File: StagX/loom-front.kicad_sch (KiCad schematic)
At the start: 11 parts

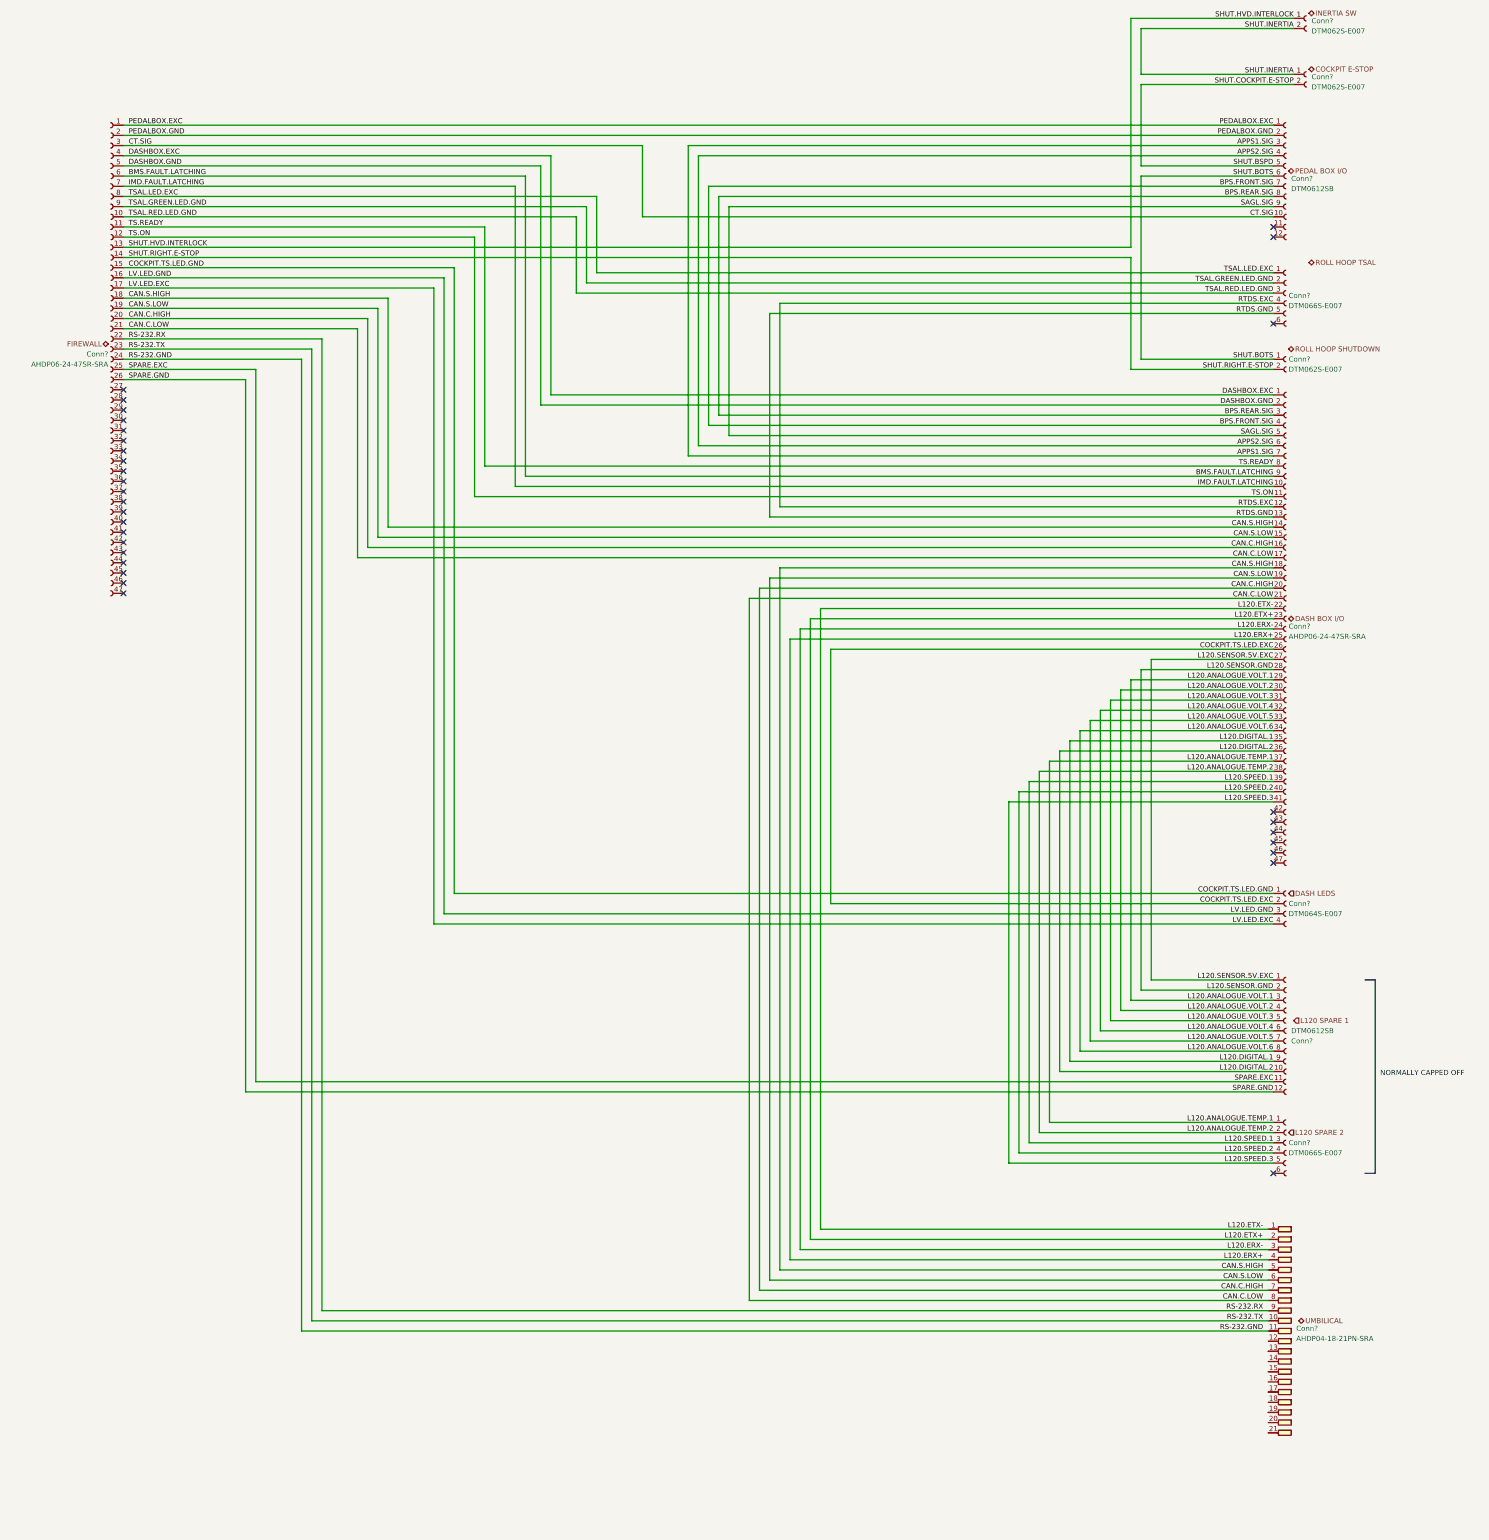
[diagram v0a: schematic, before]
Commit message: Completed shutdown loop
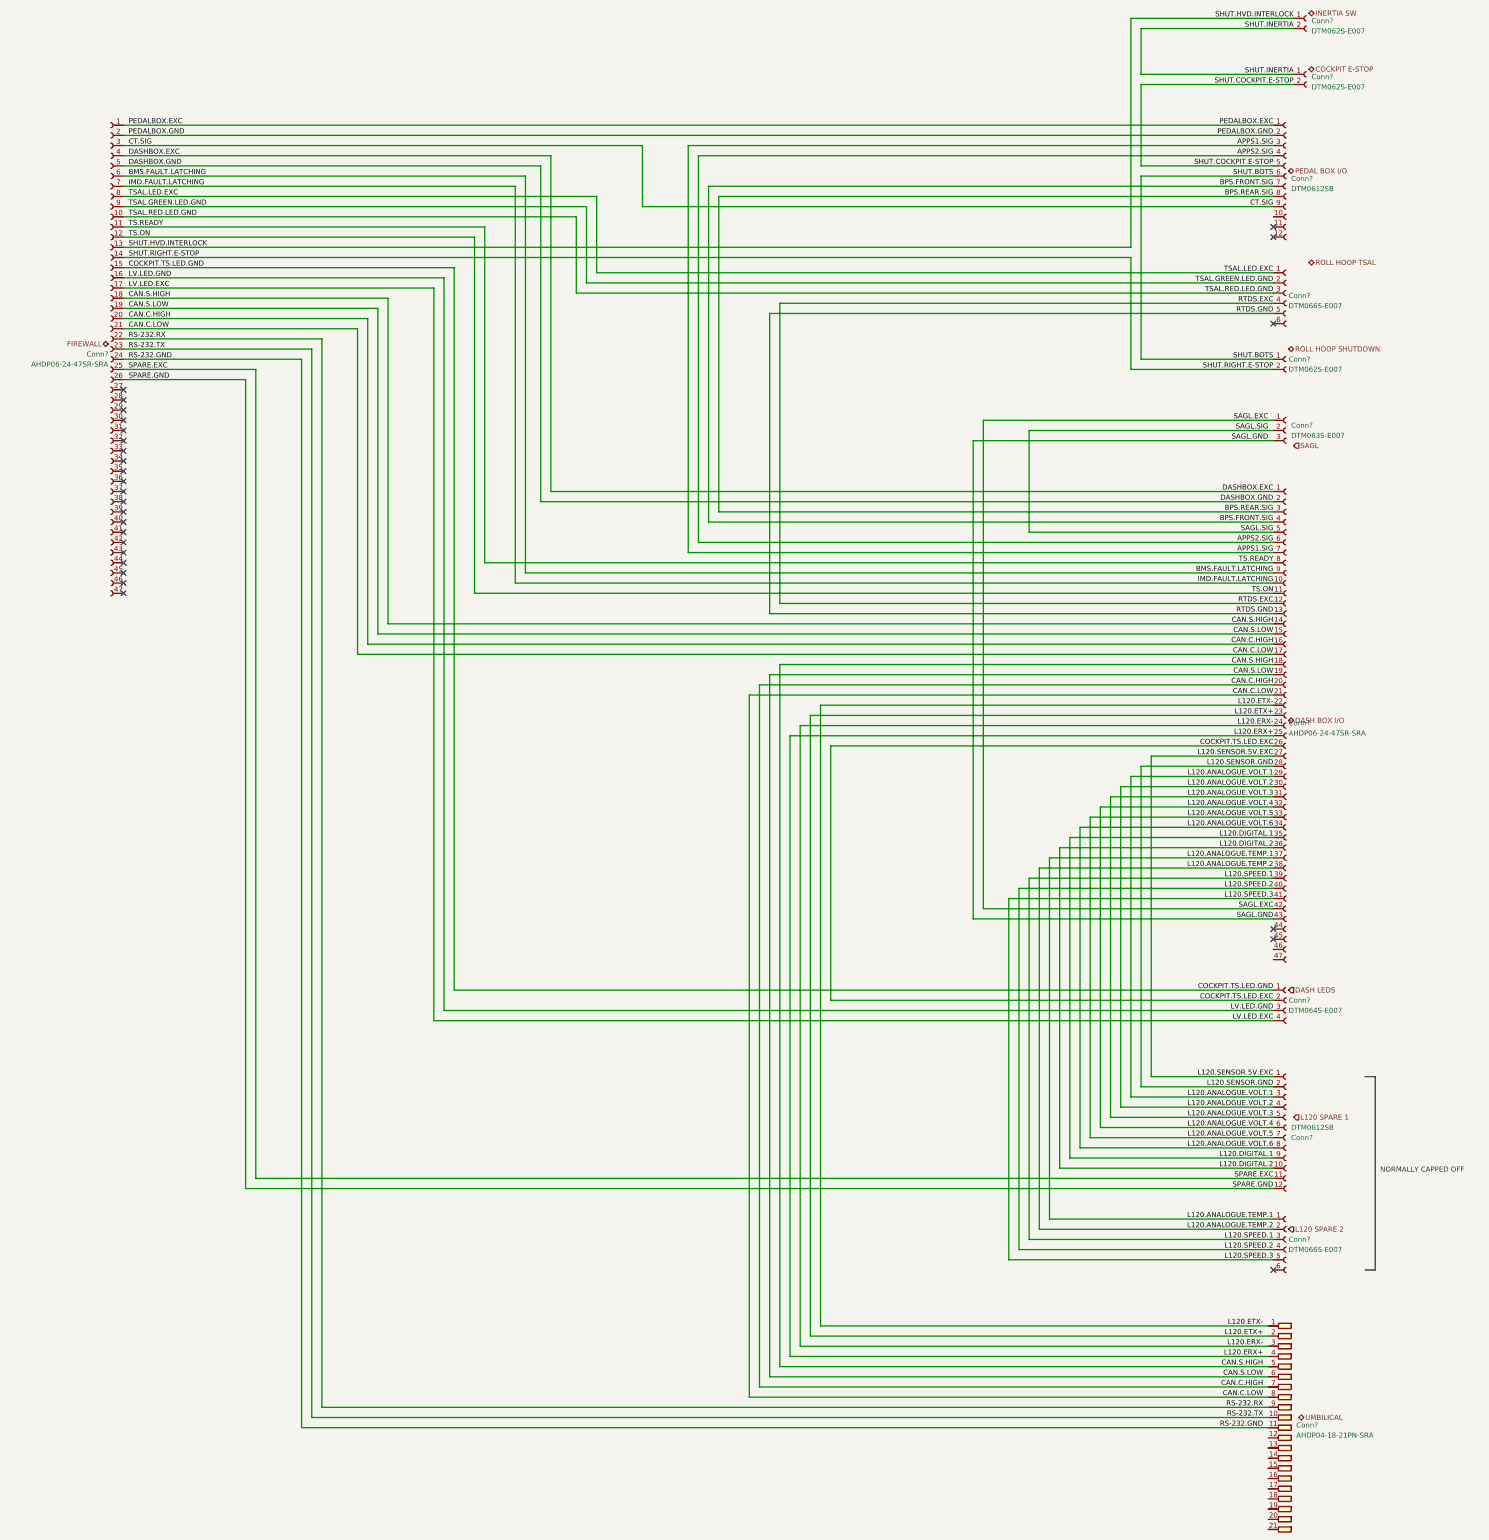
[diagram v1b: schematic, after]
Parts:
- added Conn?: Deutsch_DTM_3S_Pin, symbol Connectors_SUFST:Deutsch_DTM_3S_Pin
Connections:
- net CT.SIG: now also Conn?.9; no longer Conn?.10
- net SAGL.SIG: now also Conn?.2; no longer Conn?.9
- net SAGL.EXC: now reaches Conn?.42
- net SAGL.EXC: now also Conn?.1
- net SAGL.GND: now reaches Conn?.43
- net SAGL.GND: now also Conn?.3
- net SHUT.BSPD renamed SHUT.COCKPIT.E-STOP
- no-connect marks 31 -> 27
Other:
- moved on the sheet: Conn?

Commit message: Post comp commit
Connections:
- net COCKPIT.TS.LED.EXC: no longer Conn?.2
- net BSPD.CUR_SEN.EXC: now reaches Conn?.10
- net BSPD.CUR_SEN.EXC: now also Conn?.27
- net BSPD.CUR_SEN.GND: now reaches Conn?.11
- net BSPD.CUR_SEN.GND: now also Conn?.28
- net COCKPIT.TS_OFF.LED.GND: now reaches Conn?.29
- net COCKPIT.TS_OFF.LED.GND: now also Conn?.2
- no-connect marks 27 -> 24
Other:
- note added: "NC at "DASH LEDs" conn"
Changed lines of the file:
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@@
 	)
 	(no_connect
-		(at 58.42 120.65)
-	)
-	(no_connect
 		(at 345.44 99.06)
 	)
@@
 	)
 	(no_connect
-		(at 58.42 118.11)
+		(at 58.42 153.67)
 	)
 	(no_connect
-		(at 58.42 153.67)
+		(at 234.95 257.81)
 	)
 	(no_connect
@@
 	)
 	(no_connect
-		(at 345.44 74.93)
-	)
-	(no_connect
 		(at 345.44 335.28)
 	)
@@
 	)
 	(no_connect
-		(at 58.42 115.57)
-	)
-	(no_connect
 		(at 58.42 140.97)
 	)
@@
 	(wire
 		(pts
+			(xy 81.28 120.65) (xy 58.42 120.65)
+		)
+		(stroke
+			(width 0)
+			(type default)
+		)
+	)
+	(wire
+		(pts
 			(xy 345.44 196.85) (xy 229.87 196.85)
 		)
@@
 	(wire
 		(pts
+			(xy 275.59 115.57) (xy 275.59 72.39)
+		)
+		(stroke
+			(width 0)
+			(type default)
+		)
+	)
+	(wire
+		(pts
 			(xy 314.96 287.02) (xy 345.44 287.02)
 		)
@@
 	(wire
 		(pts
+			(xy 345.44 267.97) (xy 81.28 267.97)
+		)
+		(stroke
+			(width 0)
+			(type default)
+		)
+	)
+	(wire
+		(pts
 			(xy 58.42 105.41) (xy 105.41 105.41)
 		)
@@
 	(wire
 		(pts
+			(xy 234.95 204.47) (xy 234.95 257.81)
+		)
+		(stroke
+			(width 0)
+			(type default)
+		)
+	)
+	(wire
+		(pts
 			(xy 148.59 74.93) (xy 148.59 158.75)
 		)
@@
 	(wire
 		(pts
+			(xy 81.28 267.97) (xy 81.28 120.65)
+		)
+		(stroke
+			(width 0)
+			(type default)
+		)
+	)
+	(wire
+		(pts
 			(xy 292.1 309.88) (xy 292.1 229.87)
 		)
@@
 	(wire
 		(pts
+			(xy 275.59 72.39) (xy 345.44 72.39)
+		)
+		(stroke
+			(width 0)
+			(type default)
+		)
+	)
+	(wire
+		(pts
 			(xy 345.44 322.58) (xy 289.56 322.58)
 		)
@@
 	(wire
 		(pts
+			(xy 345.44 74.93) (xy 278.13 74.93)
+		)
+		(stroke
+			(width 0)
+			(type default)
+		)
+	)
+	(wire
+		(pts
 			(xy 270.51 128.27) (xy 345.44 128.27)
 		)
@@
 	(wire
 		(pts
+			(xy 278.13 74.93) (xy 278.13 118.11)
+		)
+		(stroke
+			(width 0)
+			(type default)
+		)
+	)
+	(wire
+		(pts
 			(xy 273.05 245.11) (xy 273.05 123.19)
 		)
@@
 	(wire
 		(pts
-			(xy 234.95 267.97) (xy 345.44 267.97)
+			(xy 345.44 54.61) (xy 199.39 54.61)
 		)
 		(stroke
@@
 	(wire
 		(pts
-			(xy 345.44 54.61) (xy 199.39 54.61)
+			(xy 278.13 118.11) (xy 58.42 118.11)
 		)
 		(stroke
@@
 	(wire
 		(pts
+			(xy 58.42 115.57) (xy 275.59 115.57)
+		)
+		(stroke
+			(width 0)
+			(type default)
+		)
+	)
+	(wire
+		(pts
 			(xy 148.59 158.75) (xy 345.44 158.75)
 		)
@@
 	(wire
 		(pts
-			(xy 234.95 204.47) (xy 234.95 267.97)
-		)
-		(stroke
-			(width 0)
-			(type default)
-		)
-	)
-	(wire
-		(pts
 			(xy 345.44 186.69) (xy 219.71 186.69)
 		)
@@
 		)
 	)
+	(text "NC at \"DASH LEDs\" conn"
+		(exclude_from_sim no)
+		(at 248.92 257.81 0)
+		(effects
+			(font
+				(size 1.27 1.27)
+			)
+		)
+	)
 	(label "DASHBOX.GND"
 		(at 59.69 59.69 0)
@@
 		)
 	)
+	(label "BSPD.CUR_SEN.GND"
+		(at 345.44 74.93 180)
+		(fields_autoplaced yes)
+		(effects
+			(font
+				(size 1.27 1.27)
+			)
+			(justify right bottom)
+		)
+	)
 	(label "CAN.S.LOW"
 		(at 345.44 186.69 180)
@@
 		)
 	)
+	(label "TSAC.HVS.GND"
+		(at 59.69 120.65 0)
+		(fields_autoplaced yes)
+		(effects
+			(font
+				(size 1.27 1.27)
+			)
+			(justify left bottom)
+		)
+	)
 	(label "L120.SPEED.2"
 		(at 345.44 240.03 180)
@@
 		)
 	)
+	(label "BSPD.CUR_SEN.EXC"
+		(at 345.44 72.39 180)
+		(fields_autoplaced yes)
+		(effects
+			(font
+				(size 1.27 1.27)
+			)
+			(justify right bottom)
+		)
+	)
 	(label "L120.ANALOGUE.TEMP.1"
 		(at 345.44 322.58 180)
@@
 		)
 	)
+	(label "BSPD.CUR_SEN.EXC"
+		(at 59.69 115.57 0)
+		(fields_autoplaced yes)
+		(effects
+			(font
+				(size 1.27 1.27)
+			)
+			(justify left bottom)
+		)
+	)
 	(label "TSAL.RED.LED.GND"
 		(at 59.69 72.39 0)
@@
 		)
 	)
+	(label "BSPD.CUR_SEN.GND"
+		(at 59.69 118.11 0)
+		(fields_autoplaced yes)
+		(effects
+			(font
+				(size 1.27 1.27)
+			)
+			(justify left bottom)
+		)
+	)
 	(label "SHUT.COCKPIT.E-STOP"
 		(at 345.44 59.69 180)
@@
 		)
 	)
+	(label "COCKPIT.TS_OFF.LED.GND"
+		(at 345.44 267.97 180)
+		(fields_autoplaced yes)
+		(effects
+			(font
+				(size 1.27 1.27)
+			)
+			(justify right bottom)
+		)
+	)
 	(label "CT.SIG"
 		(at 345.44 69.85 180)
@@
 		)
 	)
-	(label "COCKPIT.TS.LED.EXC"
-		(at 345.44 267.97 180)
-		(fields_autoplaced yes)
-		(effects
-			(font
-				(size 1.27 1.27)
-			)
-			(justify right bottom)
-		)
-	)
 	(label "SHUT.RIGHT.E-STOP"
 		(at 59.69 82.55 0)
@@
 	(hierarchical_label "ROLL HOOP TSAL"
 		(shape bidirectional)
-		(at 354.33 83.82 0)
+		(at 351.79 88.9 0)
 		(fields_autoplaced yes)
 		(effects
